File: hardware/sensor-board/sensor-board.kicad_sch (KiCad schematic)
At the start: 43 parts, among them J1 QWIIC Connector, J2 QWIIC Connector, J3 3-pole terminal, J4 2-pole terminal, Q1 BSS84, SW1 SW_DIP_x03, U1 DS18B20, U2 DS2482S-100+, U3 PCA9501PW_118, U4 LMV601, U5 MCP96L01T-E{slash}MX, U6 ADS7823EB{slash}250

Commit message: Changed solder pad style, added in the Sensor EEPROM init
- of course, no boards hooked up yet, so it properly detects it.
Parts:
- JP1, JP2, JP5, JP6: footprint Jumper:SolderJumper-3_P1.3mm_Open_RoundedPad1.0x1.5mm -> Jumper:SolderJumper-3_P2.0mm_Open_TrianglePad1.0x1.5mm
- JP3, JP4: footprint Jumper:SolderJumper-2_P1.3mm_Open_RoundedPad1.0x1.5mm -> Jumper:SolderJumper-2_P1.3mm_Open_TrianglePad1.0x1.5mm
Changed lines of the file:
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@@
       (effects (font (size 1.27 1.27)) (justify left))
     )
-    (property "Footprint" "Jumper:SolderJumper-3_P1.3mm_Open_RoundedPad1.0x1.5mm" (id 2) (at 103.886 172.339 0)
+    (property "Footprint" "Jumper:SolderJumper-3_P2.0mm_Open_TrianglePad1.0x1.5mm" (id 2) (at 103.886 172.339 0)
       (effects (font (size 1.27 1.27)) hide)
     )
@@
       (effects (font (size 1.27 1.27)) (justify left))
     )
-    (property "Footprint" "Jumper:SolderJumper-3_P1.3mm_Open_RoundedPad1.0x1.5mm" (id 2) (at 255.016 140.208 0)
+    (property "Footprint" "Jumper:SolderJumper-3_P2.0mm_Open_TrianglePad1.0x1.5mm" (id 2) (at 255.016 140.208 0)
       (effects (font (size 1.27 1.27)) hide)
     )
@@
     (property "Reference" "JP3" (id 0) (at 133.858 46.228 0))
     (property "Value" "Solder Jumper" (id 1) (at 133.858 48.768 0))
-    (property "Footprint" "Jumper:SolderJumper-2_P1.3mm_Open_RoundedPad1.0x1.5mm" (id 2) (at 133.858 52.324 0)
+    (property "Footprint" "Jumper:SolderJumper-2_P1.3mm_Open_TrianglePad1.0x1.5mm" (id 2) (at 133.858 52.324 0)
       (effects (font (size 1.27 1.27)) hide)
     )
@@
       (effects (font (size 1.27 1.27)) (justify left))
     )
-    (property "Footprint" "Jumper:SolderJumper-3_P1.3mm_Open_RoundedPad1.0x1.5mm" (id 2) (at 97.155 163.322 0)
+    (property "Footprint" "Jumper:SolderJumper-3_P2.0mm_Open_TrianglePad1.0x1.5mm" (id 2) (at 97.155 163.322 0)
       (effects (font (size 1.27 1.27)) hide)
     )
@@
       (effects (font (size 1.27 1.27)) (justify left))
     )
-    (property "Footprint" "Jumper:SolderJumper-3_P1.3mm_Open_RoundedPad1.0x1.5mm" (id 2) (at 188.214 142.24 0)
+    (property "Footprint" "Jumper:SolderJumper-3_P2.0mm_Open_TrianglePad1.0x1.5mm" (id 2) (at 188.214 142.24 0)
       (effects (font (size 1.27 1.27)) hide)
     )
@@
     (property "Reference" "JP4" (id 0) (at 133.985 63.627 0))
     (property "Value" "Solder Jumper" (id 1) (at 134.112 65.405 0))
-    (property "Footprint" "Jumper:SolderJumper-2_P1.3mm_Open_RoundedPad1.0x1.5mm" (id 2) (at 133.858 59.944 0)
+    (property "Footprint" "Jumper:SolderJumper-2_P1.3mm_Open_TrianglePad1.0x1.5mm" (id 2) (at 133.858 59.944 0)
       (effects (font (size 1.27 1.27)) hide)
     )
@@
     )
     (path "/595a5caa-76d9-4085-8241-3163330acba3"
-      (reference "JP1") (unit 1) (value "AD0 Jumper") (footprint "Jumper:SolderJumper-3_P1.3mm_Open_RoundedPad1.0x1.5mm")
+      (reference "JP1") (unit 1) (value "AD0 Jumper") (footprint "Jumper:SolderJumper-3_P2.0mm_Open_TrianglePad1.0x1.5mm")
     )
     (path "/292f5e1b-fbb3-4f2d-8132-499def51a324"
-      (reference "JP2") (unit 1) (value "AD1 Jumper") (footprint "Jumper:SolderJumper-3_P1.3mm_Open_RoundedPad1.0x1.5mm")
+      (reference "JP2") (unit 1) (value "AD1 Jumper") (footprint "Jumper:SolderJumper-3_P2.0mm_Open_TrianglePad1.0x1.5mm")
     )
     (path "/46122124-145c-415d-b404-5480beb7a4f5"
-      (reference "JP3") (unit 1) (value "Solder Jumper") (footprint "Jumper:SolderJumper-2_P1.3mm_Open_RoundedPad1.0x1.5mm")
+      (reference "JP3") (unit 1) (value "Solder Jumper") (footprint "Jumper:SolderJumper-2_P1.3mm_Open_TrianglePad1.0x1.5mm")
     )
     (path "/ea00bd9f-3929-4ec2-ad28-a2b4fd4c60bc"
-      (reference "JP4") (unit 1) (value "Solder Jumper") (footprint "Jumper:SolderJumper-2_P1.3mm_Open_RoundedPad1.0x1.5mm")
+      (reference "JP4") (unit 1) (value "Solder Jumper") (footprint "Jumper:SolderJumper-2_P1.3mm_Open_TrianglePad1.0x1.5mm")
     )
     (path "/62980e78-1006-4777-b867-c0deb5768d46"
-      (reference "JP5") (unit 1) (value "A0 Jumper") (footprint "Jumper:SolderJumper-3_P1.3mm_Open_RoundedPad1.0x1.5mm")
+      (reference "JP5") (unit 1) (value "A0 Jumper") (footprint "Jumper:SolderJumper-3_P2.0mm_Open_TrianglePad1.0x1.5mm")
     )
     (path "/368c8063-1553-4299-b6a2-80fc81df3b1a"
-      (reference "JP6") (unit 1) (value "A1 Jumper") (footprint "Jumper:SolderJumper-3_P1.3mm_Open_RoundedPad1.0x1.5mm")
+      (reference "JP6") (unit 1) (value "A1 Jumper") (footprint "Jumper:SolderJumper-3_P2.0mm_Open_TrianglePad1.0x1.5mm")
     )
     (path "/69297ace-f2f0-4cb1-a491-a8c8c194a49e"

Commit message: Change coolant sensor to a 10k NTC thermistor
- this requires one more "TBD" resistor to be added to the board.
- regenerated gerbers
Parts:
- added R6: TBD, Resistor_SMD:R_0805_2012Metric_Pad1.20x1.40mm_HandSolder, symbol Device:R
- renumbered R9 to R10, R10 to R11, R11 to R12, R12 to R13, R13 to R14, R14 to R15, R6 to R7, R7 to R8, R8 to R9
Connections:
- net +3V3A: now also R6.1
- net at D3.1 (K), R4.2, R7.1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: now also R6.2
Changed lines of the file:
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@@
+    (stroke (width 0) (type default) (color 0 0 0 0))
+  )
+  (wire (pts (xy 118.999 113.665) (xy 118.999 115.57))
     (stroke (width 0) (type default) (color 0 0 0 0))
   )
@@
     (stroke (width 0) (type default) (color 0 0 0 0))
   )
+  (wire (pts (xy 117.221 113.665) (xy 118.999 113.665))
+    (stroke (width 0) (type default) (color 0 0 0 0))
+  )
   (wire (pts (xy 149.098 143.51) (xy 167.132 143.51))
     (stroke (width 0) (type default) (color 0 0 0 0))
@@
   )
   (wire (pts (xy 87.884 30.734) (xy 98.552 30.734))
+    (stroke (width 0) (type default) (color 0 0 0 0))
+  )
+  (wire (pts (xy 118.999 123.19) (xy 118.999 128.27))
     (stroke (width 0) (type default) (color 0 0 0 0))
   )
@@
   (text "I2C Address 0x60-67" (at 192.786 83.82 0)
     (effects (font (size 1.27 1.27)) (justify left bottom))
+  )
+  (global_label "+3V3A" (shape input) (at 117.221 113.665 180) (fields_autoplaced)
+    (effects (font (size 1.27 1.27)) (justify right))
+    (property "Intersheet References" "${INTERSHEET_REFS}" (id 0) (at 108.6393 113.5856 0)
+      (effects (font (size 1.27 1.27)) (justify right) hide)
+    )
   )
   (global_label "SCL" (shape bidirectional) (at 24.13 183.515 180) (fields_autoplaced)
@@
   (symbol (lib_id "Device:R") (at 148.336 47.244 0) (unit 1)
     (in_bom yes) (on_board yes) (fields_autoplaced)
-    (property "Reference" "R9" (id 0) (at 150.368 45.9739 0)
+    (property "Reference" "R10" (id 0) (at 150.368 45.9739 0)
       (effects (font (size 1.27 1.27)) (justify left))
     )
@@
   (symbol (lib_id "Device:R") (at 122.682 91.948 0) (unit 1)
     (in_bom yes) (on_board yes) (fields_autoplaced)
-    (property "Reference" "R7" (id 0) (at 125.476 90.6779 0)
+    (property "Reference" "R8" (id 0) (at 125.476 90.6779 0)
       (effects (font (size 1.27 1.27)) (justify left))
     )
@@
   (symbol (lib_id "Device:R") (at 118.999 134.366 0) (unit 1)
     (in_bom yes) (on_board yes)
-    (property "Reference" "R6" (id 0) (at 121.793 133.0959 0)
+    (property "Reference" "R7" (id 0) (at 121.793 133.0959 0)
       (effects (font (size 1.27 1.27)) (justify left))
     )
@@
   (symbol (lib_id "Device:R") (at 148.336 66.04 0) (unit 1)
     (in_bom yes) (on_board yes) (fields_autoplaced)
-    (property "Reference" "R10" (id 0) (at 150.876 64.7699 0)
+    (property "Reference" "R11" (id 0) (at 150.876 64.7699 0)
       (effects (font (size 1.27 1.27)) (justify left))
     )
@@
   (symbol (lib_id "Device:R") (at 156.464 66.04 0) (unit 1)
     (in_bom yes) (on_board yes) (fields_autoplaced)
-    (property "Reference" "R11" (id 0) (at 159.258 64.7699 0)
+    (property "Reference" "R12" (id 0) (at 159.258 64.7699 0)
       (effects (font (size 1.27 1.27)) (justify left))
     )
@@
   (symbol (lib_id "Device:R") (at 253.492 113.538 0) (mirror y) (unit 1)
     (in_bom yes) (on_board yes)
-    (property "Reference" "R14" (id 0) (at 251.46 112.2679 0)
+    (property "Reference" "R15" (id 0) (at 251.46 112.2679 0)
       (effects (font (size 1.27 1.27)) (justify left))
     )
@@
     (pin "2")
   )
+  (symbol (lib_id "Device:R") (at 118.999 119.38 0) (unit 1)
+    (in_bom yes) (on_board yes) (fields_autoplaced)
+    (property "Reference" "R6" (id 0) (at 121.92 118.1099 0)
+      (effects (font (size 1.27 1.27)) (justify left))
+    )
+    (property "Value" "TBD" (id 1) (at 121.92 120.6499 0)
+      (effects (font (size 1.27 1.27)) (justify left))
+    )
+    (property "Footprint" "Resistor_SMD:R_0805_2012Metric_Pad1.20x1.40mm_HandSolder" (id 2) (at 117.221 119.38 90)
+      (effects (font (size 1.27 1.27)) hide)
+    )
+    (property "Datasheet" "~" (id 3) (at 118.999 119.38 0)
+      (effects (font (size 1.27 1.27)) hide)
+    )
+    (pin "1")
+    (pin "2")
+  )
   (symbol (lib_name "GND_1") (lib_id "power:GND") (at 169.926 154.686 0) (unit 1)
     (in_bom yes) (on_board yes) (fields_autoplaced)
@@
   (symbol (lib_id "Device:R") (at 130.81 92.202 0) (unit 1)
     (in_bom yes) (on_board yes) (fields_autoplaced)
-    (property "Reference" "R8" (id 0) (at 132.842 90.9319 0)
+    (property "Reference" "R9" (id 0) (at 132.842 90.9319 0)
       (effects (font (size 1.27 1.27)) (justify left))
     )
@@
   (symbol (lib_id "Device:R") (at 242.316 67.31 0) (unit 1)
     (in_bom yes) (on_board yes) (fields_autoplaced)
-    (property "Reference" "R13" (id 0) (at 244.348 66.0399 0)
+    (property "Reference" "R14" (id 0) (at 244.348 66.0399 0)
       (effects (font (size 1.27 1.27)) (justify left))
     )
@@
   (symbol (lib_id "Device:R") (at 242.316 57.912 0) (unit 1)
     (in_bom yes) (on_board yes) (fields_autoplaced)
-    (property "Reference" "R12" (id 0) (at 244.348 56.6419 0)
+    (property "Reference" "R13" (id 0) (at 244.348 56.6419 0)
       (effects (font (size 1.27 1.27)) (justify left))
     )
@@
       (reference "R5") (unit 1) (value "10k") (footprint "Resistor_SMD:R_0805_2012Metric_Pad1.20x1.40mm_HandSolder")
     )
+    (path "/7b56b1f7-2b91-4a01-a35a-c33200eb1791"
+      (reference "R6") (unit 1) (value "TBD") (footprint "Resistor_SMD:R_0805_2012Metric_Pad1.20x1.40mm_HandSolder")
+    )
     (path "/1cb64bfe-d819-47e3-be11-515b04f2c451"
-      (reference "R6") (unit 1) (value "TBD") (footprint "Resistor_SMD:R_0805_2012Metric_Pad1.20x1.40mm_HandSolder")
+      (reference "R7") (unit 1) (value "TBD") (footprint "Resistor_SMD:R_0805_2012Metric_Pad1.20x1.40mm_HandSolder")
     )
     (path "/0551ae12-2d33-4467-b743-52f55850940f"
-      (reference "R7") (unit 1) (value "10k") (footprint "Resistor_SMD:R_0805_2012Metric_Pad1.20x1.40mm_HandSolder")
+      (reference "R8") (unit 1) (value "10k") (footprint "Resistor_SMD:R_0805_2012Metric_Pad1.20x1.40mm_HandSolder")
     )
     (path "/8cb09644-9c31-4085-b966-7fdbfa08b1f6"
-      (reference "R8") (unit 1) (value "10k") (footprint "Resistor_SMD:R_0805_2012Metric_Pad1.20x1.40mm_HandSolder")
+      (reference "R9") (unit 1) (value "10k") (footprint "Resistor_SMD:R_0805_2012Metric_Pad1.20x1.40mm_HandSolder")
     )
     (path "/010f8a10-c6fd-4247-9198-32f8f0fdec7c"
-      (reference "R9") (unit 1) (value "1M") (footprint "Resistor_SMD:R_0805_2012Metric_Pad1.20x1.40mm_HandSolder")
+      (reference "R10") (unit 1) (value "1M") (footprint "Resistor_SMD:R_0805_2012Metric_Pad1.20x1.40mm_HandSolder")
     )
     (path "/375c58d5-218c-469b-8705-d6b6f575839b"
-      (reference "R10") (unit 1) (value "2M") (footprint "Resistor_SMD:R_0805_2012Metric_Pad1.20x1.40mm_HandSolder")
+      (reference "R11") (unit 1) (value "2M") (footprint "Resistor_SMD:R_0805_2012Metric_Pad1.20x1.40mm_HandSolder")
     )
     (path "/3f3af605-6dac-46f5-bd29-4c18a05b8aff"
-      (reference "R11") (unit 1) (value "2M") (footprint "Resistor_SMD:R_0805_2012Metric_Pad1.20x1.40mm_HandSolder")
+      (reference "R12") (unit 1) (value "2M") (footprint "Resistor_SMD:R_0805_2012Metric_Pad1.20x1.40mm_HandSolder")
     )
     (path "/a8db6c56-99c9-4d71-8cbc-ce90cada5104"
-      (reference "R12") (unit 1) (value "TBD") (footprint "Resistor_SMD:R_0805_2012Metric_Pad1.20x1.40mm_HandSolder")
+      (reference "R13") (unit 1) (value "TBD") (footprint "Resistor_SMD:R_0805_2012Metric_Pad1.20x1.40mm_HandSolder")
     )
     (path "/9e64466d-e12f-4574-a1e9-834342148c0a"
-      (reference "R13") (unit 1) (value "TBD") (footprint "Resistor_SMD:R_0805_2012Metric_Pad1.20x1.40mm_HandSolder")
+      (reference "R14") (unit 1) (value "TBD") (footprint "Resistor_SMD:R_0805_2012Metric_Pad1.20x1.40mm_HandSolder")
     )
     (path "/4b0f1d88-02d0-4026-98d1-a21db9c03ff1"
-      (reference "R14") (unit 1) (value "5R") (footprint "Resistor_SMD:R_0805_2012Metric_Pad1.20x1.40mm_HandSolder")
+      (reference "R15") (unit 1) (value "5R") (footprint "Resistor_SMD:R_0805_2012Metric_Pad1.20x1.40mm_HandSolder")
     )
     (path "/0f26488d-dd08-44cf-86f5-60f9d5f43b82"

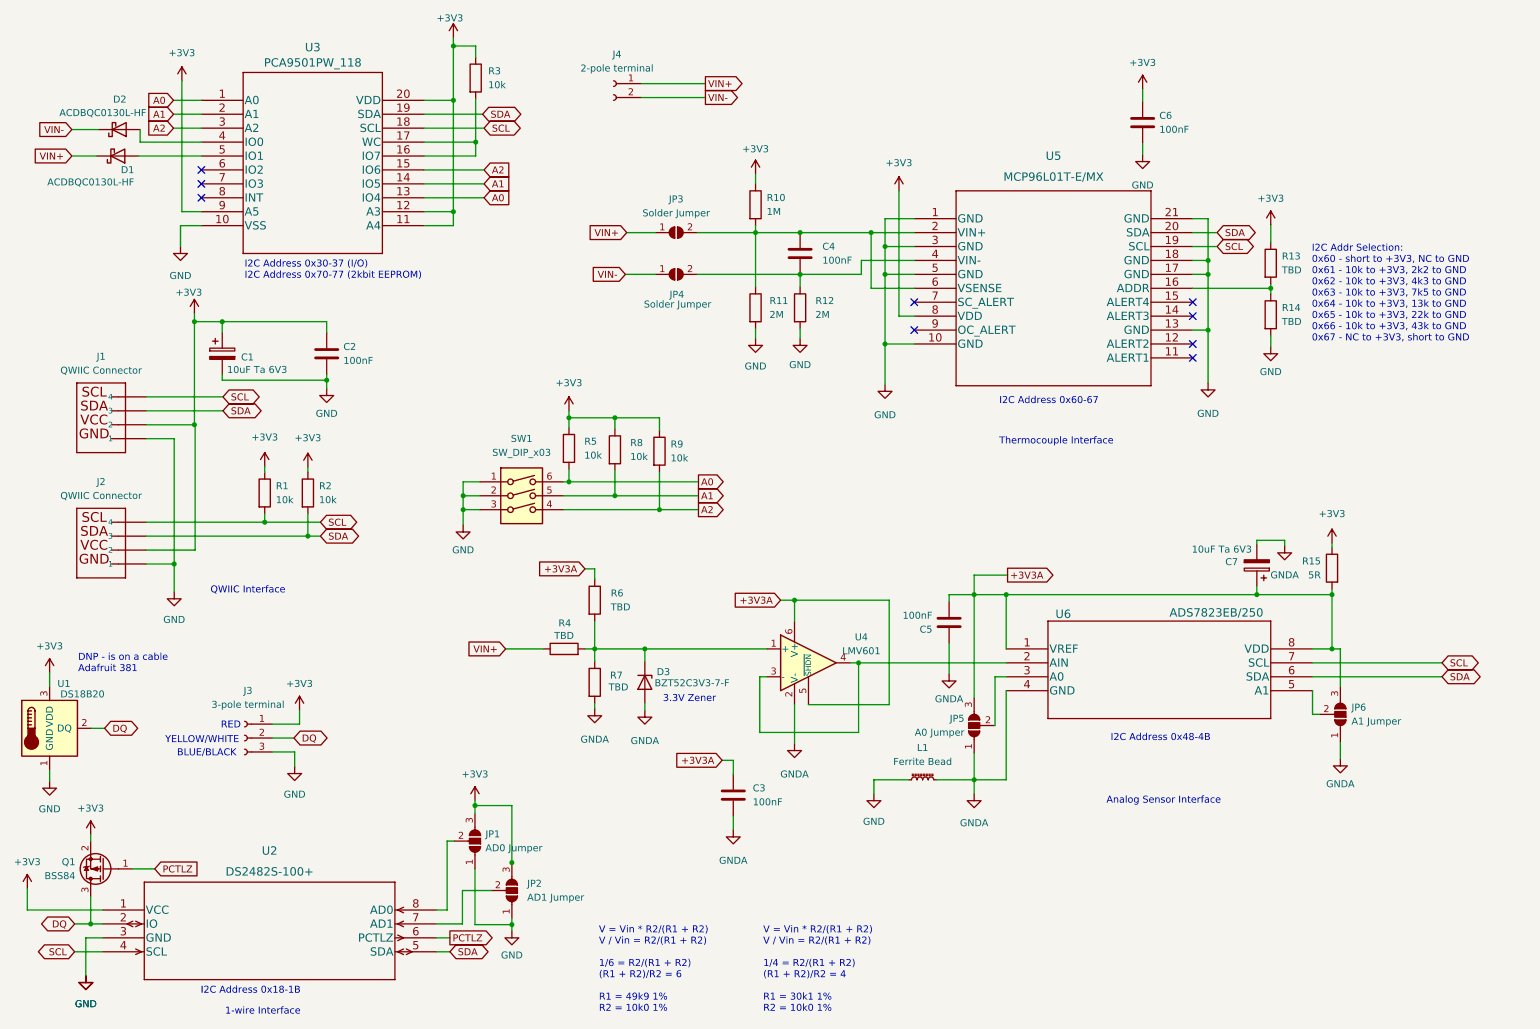
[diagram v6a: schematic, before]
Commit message: Changed DIP switch to solder jumper pads, regen gerbers
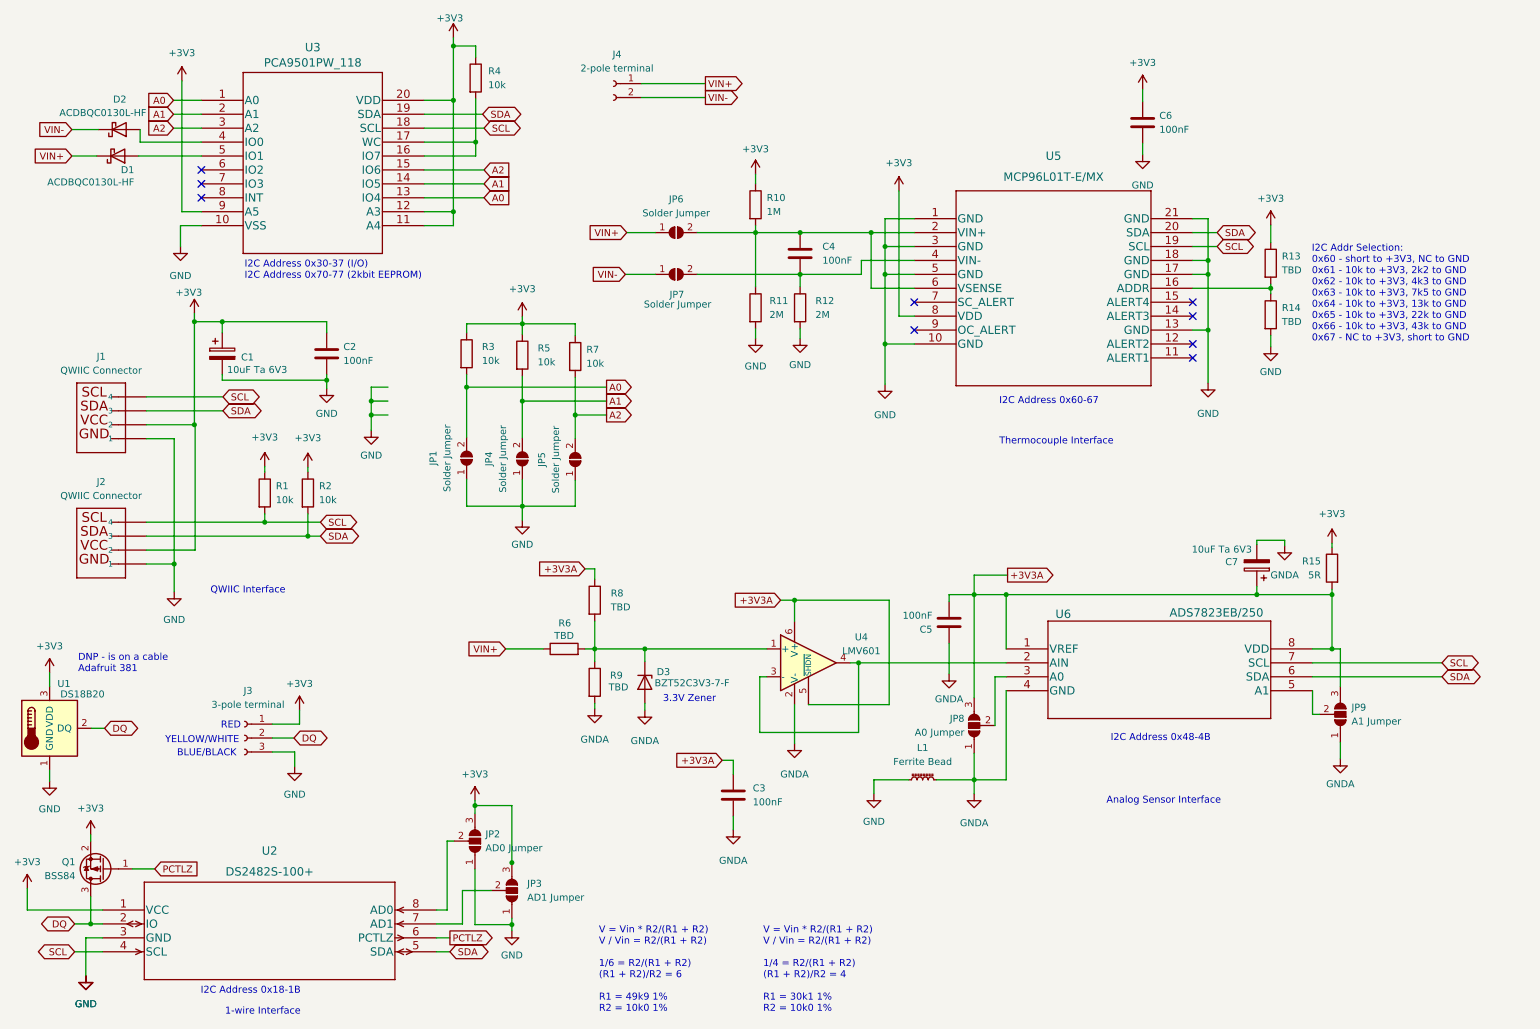
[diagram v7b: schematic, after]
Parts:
- removed SW1: SW_DIP_x03, Button_Switch_SMD:SW_DIP_SPSTx03_Slide_9.78x9.8mm_W8.61mm_P2.54mm, symbol Switch:SW_DIP_x03
- added JP1, JP4, JP5: Solder Jumper, Jumper:SolderJumper-2_P1.3mm_Open_TrianglePad1.0x1.5mm, symbol Jumper:SolderJumper_2_Open
- renumbered JP1 to JP2, JP2 to JP3, JP3 to JP6, JP4 to JP7, JP5 to JP8, JP6 to JP9, R5 to R3, R3 to R4, R8 to R5, R4 to R6, R9 to R7, R6 to R8, R7 to R9
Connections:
- net A0: now also JP1.2 (B)
- net A1: now also JP4.2 (B)
- net A2: now also JP5.2 (B)
- net GND: now also JP1.1 (A), JP4.1 (A), JP5.1 (A)
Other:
- title: (none) -> QWIIC Sensor Board
- moved on the sheet: R3, R5, R7

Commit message: Updated title block for sensor-board, add PDFs
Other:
- company: (none) -> Gavin Hurlbut
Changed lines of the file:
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@@
   (title_block
     (title "QWIIC Sensor Board")
-    (date "2023-01-29")
+    (date "2023-01-31")
     (rev "1.0")
+    (company "Gavin Hurlbut")
   )
   (junction (at 242.316 62.484) (diameter 0) (color 0 0 0 0)
